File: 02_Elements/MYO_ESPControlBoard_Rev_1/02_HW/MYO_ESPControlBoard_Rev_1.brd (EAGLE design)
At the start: 408 x 156 mm, 55 parts, among them X1 USB-MICROB

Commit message: MYO_ESPControlBoard_Rev_1 Draft Update on HW (SCH, BRD and 3D)
Primary Draft of the PCB Schematic and Layout of MYO_ESPControlBoard_Rev_1, for evaluation:

- Complete Schematic
- Draft Layout without Drills or Silk
- Primary 3D Model
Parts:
- removed C_BUZZ: 30nF, adafruit:C0805K
- removed C_UR0: 10uF, adafruit:C0805K
- removed C_UR1: 100nF, adafruit:C0805K
- removed D1: MBRA140, SparkFun-DiscreteSemi:SMA-DIODE
- removed LED_PW1: (no value), adafruit:1206
- removed L_RGB_1: (no value), SparkFun-LED:WS2812B
- removed MOTPOT_2: POLOLU_MOT_POT, PololuMotors:POLOLU_MOT_POT
- removed R_BUZZ, R_PW1: 330Ohm, adafruit:M0805
- removed R_UR0, R_UR1: 470Ohm, adafruit:M0805
- removed R_UR2, R_UR3: 12KOhm, adafruit:M0805
- removed SW_KF, SW_KU: (no value), switch-omron:B3F-31XX
- removed T_UR0, T_UR1: S8050, semicon-smd-ipc:SOT23
- removed U_BUZZ: BUZZERSMD3, SparkFun:BUZZER-CMT1102
- removed U_UR0: CH340G, ch340g:SOIC16
- removed X_UR0: 12MHz, adafruit:CTS406
- added C_AS_0, C_AS_1: 22nF, adafruit:C0805K
- added R_AS_0, R_AS_1: 4k7Ohm, adafruit:M0805
- added R_SHUNT_0, R_SHUNT_1: 0.039Ohm, adafruit:M0805
- added R_SW_3: 10kOhm, adafruit:M0805
- added SW_00, SW_EN, SW_IO0: (no value), switch-omron:B3F-10XX
- added U_AS_0, U_AS_1: ZXCT1022E5TA, ZXCT1022E5TA:SOT95P270X145-5N(SOT23-5)
- U_DR_0, U_DR_1: value L293DD -> VNH7100ASTR; device st-microelectronics:SO20 -> VNH7100ASTR:SOIC127P600X175-16N
- X1: value USB-MICROB -> 332-04; device SparkFun:USB-MICROB -> con-garry:332-04
- moved R_AXL_0 479.0 mm to (48.0, 46.0)
- moved R_AXL_SCL 474.1 mm to (48.0, 43.0)
- moved R_AXL_SDA 469.4 mm to (48.0, 40.0)
- moved U_AXL 464.1 mm to (43.0, 45.0), turned to 270 degrees
- moved SW_PW 448.6 mm to (3.00, 23.0), flipped to the bottom, turned to 90 degrees
- moved J_PW 448.5 mm to (12.0, 19.0), flipped to the bottom, turned to 180 degrees
- moved C_ESP_1 443.9 mm to (11.0, 32.0), turned to 180 degrees
- moved R_SW_1 443.7 mm to (60.0, 10.0), turned to 180 degrees
- moved R_SW_0 431.2 mm to (49.0, 10.0), turned to 180 degrees
- moved L_RGB_0 419.6 mm to (5.00, 32.0), flipped to the bottom
- moved R_ESP2 301.4 mm to (43.0, 40.0)
- moved C_ESP_2 285.3 mm to (16.0, 29.0)
- moved C_ESP_3 285.0 mm to (11.0, 29.0), turned to 180 degrees
- moved R_ESP4 279.3 mm to (16.0, 26.0), turned to 180 degrees
- moved C_VR_2 271.8 mm to (36.0, 25.0), flipped to the bottom
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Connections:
- net GPIO15 renamed GPIO15(R)
- net GPIO2 renamed SWTAC_0
- net PMOT_A_3 renamed N$6
- removed net DTR: R_UR2.1, T_UR1.2, U_UR0.13
- removed net GPIO0: R_ESP0.1, R_SW_0.2, T_UR1.3, U_ESP.25
- removed net GPIO16: U_ESP.27
- removed net MOT_A_2: MOTPOT_2.MOT_A, U_DR_1.2, U_ESP.37
- removed net MOT_A_3: U_DR_1.12
- removed net MOT_B_2: MOTPOT_2.MOT_B, U_DR_1.9, U_ESP.10
- removed net MOT_B_3: U_DR_1.19
- removed net MOT_EN_2: U_DR_1.1, U_ESP.14
- removed net MOT_EN_3: U_DR_1.11
- removed net MPOT_2: MOTPOT_2.MPOT, U_ESP.9
- removed net N$10: L_RGB_0.2, L_RGB_1.4
- removed net N$12: R_UR0.1, U_UR0.2
- removed net N$13: R_UR1.1, U_UR0.3
- removed net N$14: U_UR0.8, X_UR0.3
- removed net N$15: D1.A, X1.VBUS
- removed net N$2: U_UR0.15
- removed net N$3: R_UR3.2, T_UR1.1
- removed net N$37: U_UR0.9
- removed net N$38: U_UR0.11
- removed net N$39: U_UR0.10
- removed net N$4: R_UR2.2, T_UR0.1
- removed net N$40: U_UR0.12
- removed net N$7: U_UR0.7, X_UR0.1
- removed net N$8: LED_PW1.A, R_PW1.1
- removed net N$9: L_RGB_1.2
- removed net PMOT_A_2: U_DR_1.3
- removed net PMOT_B_2: U_DR_1.8
- removed net PMOT_B_3: U_DR_1.18
- removed net RTS: R_UR3.1, T_UR0.2, U_UR0.14
- removed net USB_D+: U_UR0.5, X1.D+
- removed net USB_D-: U_UR0.6, X1.D-
- removed net _RST: T_UR0.3
- new net GPIO0(R): R_ESP0.1, R_SW_0.2, U_ESP.25
- new net GPIO23: U_ESP.37
- new net MOT_SEN_1: U_ESP.14
- new net MSEN_0: R_AS_0.1, U_ESP.9
- new net MSEN_1: R_AS_1.1
- new net N$11: C_AS_0.1, R_AS_0.2, U_AS_0.3
- new net N$42: C_AS_1.1, R_AS_1.2, U_AS_1.3
- new net RX: X1.3
- new net SW_0: R_SW_3.2, SW_00.3, U_ESP.27
- new net SW_1: MOTPOT_1.MOT_A, U_DR_1.3, U_ESP.16
- new net TX: X1.1
- new net VCC_VR_0: C_DR_0.1, R_SHUNT_0.2, R_SHUNT_1.2, U_AS_0.5, U_DR_0.12, U_DR_0.4, U_DR_0.5
- new net VCC_VR_1: C_DR_1.1, U_AS_1.5, U_DR_1.12, U_DR_1.4, U_DR_1.5
- net 3V3: now also R_SW_3.1, X1.2; no longer MOTPOT_2.3V3, R_PW1.2
- net 5V: now also R_SHUNT_0.1, R_SHUNT_1.1, U_AS_0.4, U_AS_1.4; no longer C_DR_0.1, C_DR_1.1, L_RGB_1.1, U_DR_0.10, U_DR_0.20, U_DR_1.10, U_DR_1.20
- net BUZZER: no longer R_BUZZ.2
- net GND: now also C_AS_0.2, C_AS_1.2, SW_00.1, SW_EN.1, SW_IO0.1, U_AS_0.2, U_AS_1.2, U_DR_0.1, U_DR_0.8, U_DR_0.9, U_DR_1.1, U_DR_1.8, U_DR_1.9, X1.4; no longer C_BUZZ.2, C_UR0.2, C_UR1.2, LED_PW1.C, L_RGB_1.3, MOTPOT_2.GND, SW_KF.2, SW_KU.2, U_BUZZ.2, U_DR_0.15, U_DR_0.17, U_DR_0.4, U_DR_0.5, U_DR_0.6, U_DR_0.7, U_DR_1.15, U_DR_1.17, U_DR_1.4, U_DR_1.5, U_DR_1.6, U_DR_1.7, U_UR0.1, X1.GND
- net MOT_A_0: now also U_DR_0.3; no longer U_DR_0.2
- net MOT_A_1: now also U_ESP.10; no longer MOTPOT_1.MOT_A, U_DR_0.12, U_ESP.16
- net MOT_B_0: now also U_DR_0.6; no longer U_DR_0.9
- net MOT_B_1: now also U_DR_1.6; no longer U_DR_0.19
- net MOT_EN_0: now also U_DR_0.11; no longer U_DR_0.1
- net MOT_EN_1: now also U_DR_1.11; no longer U_DR_0.11
- net N$1: now also U_DR_0.13; no longer C_BUZZ.1, R_BUZZ.1, U_BUZZ.1
- net N$18: now also SW_EN.3; no longer SW_KU.1
- net N$19: now also SW_IO0.3; no longer SW_KF.1
- net PMOT_A_0: now also U_DR_0.15, U_DR_0.2; no longer U_DR_0.3
- net PMOT_A_1: now also U_DR_1.15, U_DR_1.2; no longer U_DR_0.13
- net PMOT_B_0: now also U_DR_0.10, U_DR_0.7; no longer U_DR_0.8
- net PMOT_B_1: now also U_DR_1.10, U_DR_1.7; no longer U_DR_0.18
- net RXD: no longer R_UR1.2
- net TXD: no longer R_UR0.2
- net VIN: no longer C_UR0.1, C_UR1.1, D1.C, U_UR0.16
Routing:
- net GND: track 0.00 -> 330.0 mm, vias 0 -> 11
- net 3V3: track 0.00 -> 162.3 mm, vias 0 -> 6
- net 5V: track 0.00 -> 124.7 mm, vias 0 -> 3
- net VCC_VR_0: track 0.00 -> 117.4 mm, vias 0 -> 2
- net MOT_EN_0: track 0.00 -> 83.0 mm, vias 0 -> 2
- net MSEN_0: track 0.00 -> 74.8 mm, vias 0 -> 2
- net VIN: track 0.00 -> 73.3 mm, vias 0 -> 3
- net MPOT_0: track 0.00 -> 73.0 mm
- net MOT_A_0: track 0.00 -> 72.0 mm, vias 0 -> 6
- net MOT_EN_1: track 0.00 -> 70.2 mm
- net EN: track 0.00 -> 69.7 mm
- net MOT_B_0: track 0.00 -> 63.8 mm, vias 0 -> 5
- net SCL: track 0.00 -> 53.3 mm, vias 0 -> 3
- net GPIO0(R): track 0.00 -> 44.0 mm, vias 0 -> 3
- net SDA: track 0.00 -> 41.7 mm, vias 0 -> 4
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- removed copper zone on layer 1, net GND
- removed copper zone on layer 16, net GND
- removed copper zone on layer 16, net N$11
- removed copper zone on layer 1, net N$6 (its old number)
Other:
- board size 408 x 156 mm -> 72 x 57 mm
- board text removed: "Add a dissipator to avoid overheating"
- board text removed: "BOT:"
- board text removed: "C:/Users/PablodMM/Google Drive/Henar #3/03_Recursos/License_3_0_Logo.bmp"
- board text removed: "C_MUX_0"
- board text removed: "C_MUX_1"
- board text removed: "C_VR_1"
- board text removed: "Check the Fuse in case the board is not powered"
- board text removed: "F_PW"
- board text removed: "GND 5V RX TX"
- board text removed: "GND 5V_ARD MUX_D MUX_C MUX_B MUX_A MUX_2"
- board text removed: "H3_MIDIController_Rev_3_MainBoard"
- board text removed: "J_MIDI"
- board text removed: "J_SW_00"
- board text removed: "J_SW_01"
- board text removed: "J_SW_02"
- board text removed: "J_SW_03"
- board text removed: "J_SW_04"
- board text removed: "J_SW_05"
- board text removed: "J_SW_06"
- board text removed: "J_SW_07"
- board text removed: "J_SW_08"
- board text removed: "J_SW_09"
- board text removed: "J_SW_10"
- board text removed: "J_SW_11"
- board text removed: "J_SW_12"
- board text removed: "J_SW_13"
- board text removed: "J_SW_14"
- board text removed: "J_SW_15"
- board text removed: "J_SW_16"
- board text removed: "J_SW_17"
- board text removed: "J_SW_18"
- board text removed: "J_SW_19"
- board text removed: "J_SW_20"
- board text removed: "J_SW_21"
- board text removed: "J_SW_22"
- board text removed: "J_SW_23"
- board text removed: "J_SW_24"
- board text removed: "J_SW_25"
- board text removed: "J_SW_26"
- board text removed: "J_SW_27"
- board text removed: "J_SW_28"
- board text removed: "J_SW_29"
- board text removed: "J_SW_30"
- board text removed: "J_SW_31"
- board text removed: "LED_IN LED_OUT 5V GND SW_00"
- board text removed: "LED_IN LED_OUT 5V GND SW_01"
- board text removed: "LED_IN LED_OUT 5V GND SW_02"
- board text removed: "LED_IN LED_OUT 5V GND SW_03"
- board text removed: "LED_IN LED_OUT 5V GND SW_04"
- board text removed: "LED_IN LED_OUT 5V GND SW_05"
- board text removed: "LED_IN LED_OUT 5V GND SW_06"
- board text removed: "LED_IN LED_OUT 5V GND SW_07"
- board text removed: "LED_IN LED_OUT 5V GND SW_08"
- board text removed: "LED_IN LED_OUT 5V GND SW_09"
- board text removed: "LED_IN LED_OUT 5V GND SW_10"
- board text removed: "LED_IN LED_OUT 5V GND SW_13"
- board text removed: "LED_IN LED_OUT 5V GND SW_14"
- board text removed: "LED_IN LED_OUT 5V GND SW_15"
- board text removed: "LED_IN LED_OUT 5V GND SW_16"
- board text removed: "LED_IN LED_OUT 5V GND SW_17"
- board text removed: "LED_IN LED_OUT 5V GND SW_18"
- board text removed: "LED_IN LED_OUT 5V GND SW_19"
- board text removed: "LED_IN LED_OUT 5V GND SW_20"
- board text removed: "LED_IN LED_OUT 5V GND SW_21"
- board text removed: "LED_IN LED_OUT 5V GND SW_22"
- board text removed: "LED_IN LED_OUT 5V GND SW_23"
- board text removed: "LED_IN LED_OUT 5V GND SW_24"
- board text removed: "LED_IN LED_OUT 5V GND SW_25"
- board text removed: "LED_IN LED_OUT 5V GND SW_26"
- board text removed: "LED_IN LED_OUT 5V GND SW_29"
- board text removed: "LED_IN LED_OUT 5V GND SW_30"
- board text removed: "LED_IN LED_OUT 5V GND SW_31"
- board text removed: "LED_PW"
- board text removed: "LED_RGB"
- board text removed: "Licensed CC BY-SA 3.0"
- board text removed: "Multiplexer 16to1 MUX_0"
- board text removed: "Multiplexer 16to1 MUX_1"
- board text removed: "RAW(NC) GND RST(NC) 5V_ARD A3(NC) MUX_2 MUX_1 MUX_0 D13(NC) D12(NC) D11(NC) D10(NC)"
- board text removed: "R_LED_B"
- board text removed: "R_LED_G"
- board text removed: "R_LED_R"
- board text removed: "R_MIDI_0"
- board text removed: "R_MIDI_1"
- board text removed: "R_MIDI_2"
- board text removed: "R_PW"
- board text removed: "SWPad 00"
- board text removed: "SWPad 01"
- board text removed: "SWPad 02"
- board text removed: "SWPad 03"
- board text removed: "SWPad 04"
- board text removed: "SWPad 05"
- board text removed: "SWPad 06"
- board text removed: "SWPad 07"
- board text removed: "SWPad 08"
- board text removed: "SWPad 09"
- board text removed: "SWPad 10"
- board text removed: "SWPad 11"
- board text removed: "SWPad 12"
- board text removed: "SWPad 13"
- board text removed: "SWPad 14"
- board text removed: "SWPad 15"
- board text removed: "SWPad 16"
- board text removed: "SWPad 17"
- board text removed: "SWPad 18"
- board text removed: "SWPad 19"
- board text removed: "SWPad 20"
- board text removed: "SWPad 21"
- board text removed: "SWPad 22"
- board text removed: "SWPad 23"
- board text removed: "SWPad 24"
- board text removed: "SWPad 25"
- board text removed: "SWPad 26"
- board text removed: "SWPad 27"
- board text removed: "SWPad 28"
- board text removed: "SWPad 29"
- board text removed: "SWPad 30"
- board text removed: "SWPad 31"
- board text removed: "Spain, 2017"
- board text removed: "TX RX 5V GND"
- board text removed: "U_MUX_0"
- board text removed: "U_MUX_1"
- board text removed: "U_VR_5V"
- board text removed: "VIN GND VOUT"

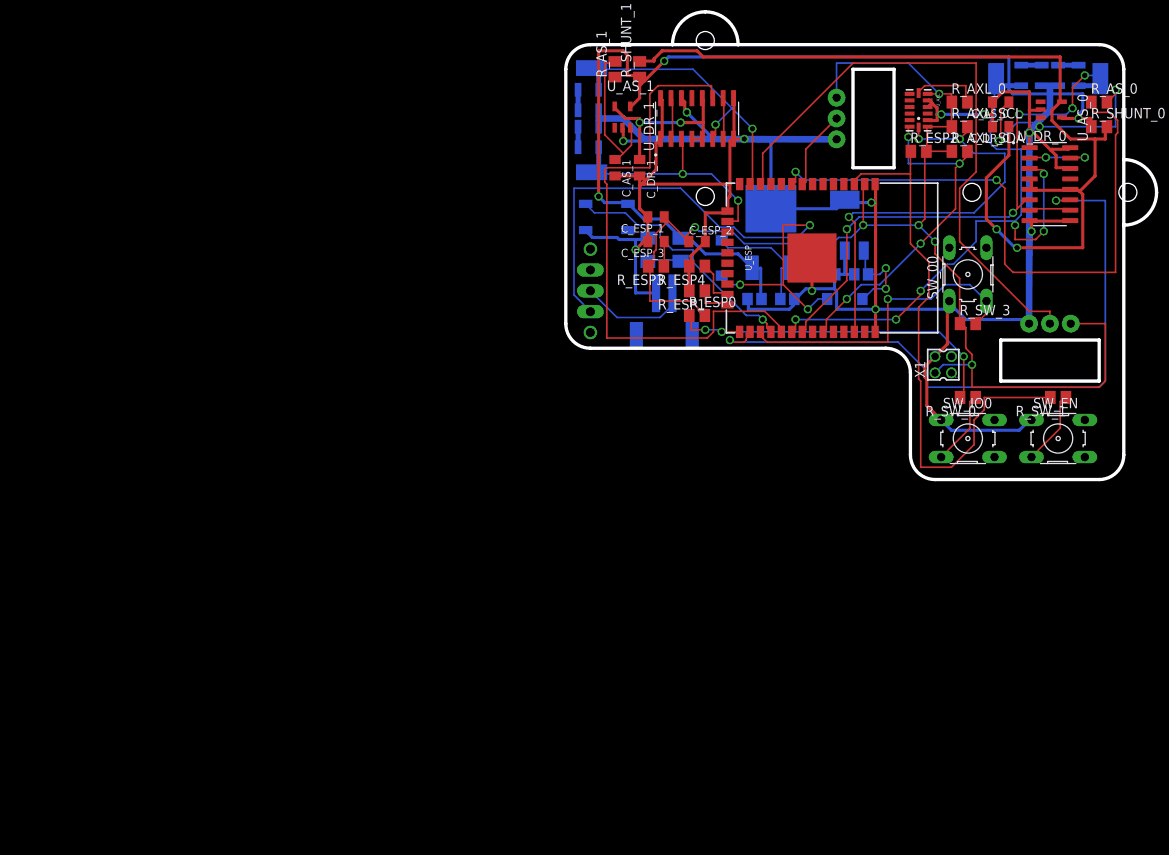
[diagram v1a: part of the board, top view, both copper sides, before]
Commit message: Updated Design with NPN JTAG Programming Interface
Changed Schematic:

- Added NPN JTAG Controller (as for https://dl.espressif.com/dl/schematics/ESP32-Core-Board-V2_sch.pdf ). Suppresed 2 Tactile Switches for Programming Interface
- Added 1 Tactile Switch for User Interface
- Added Expressiv Documentation
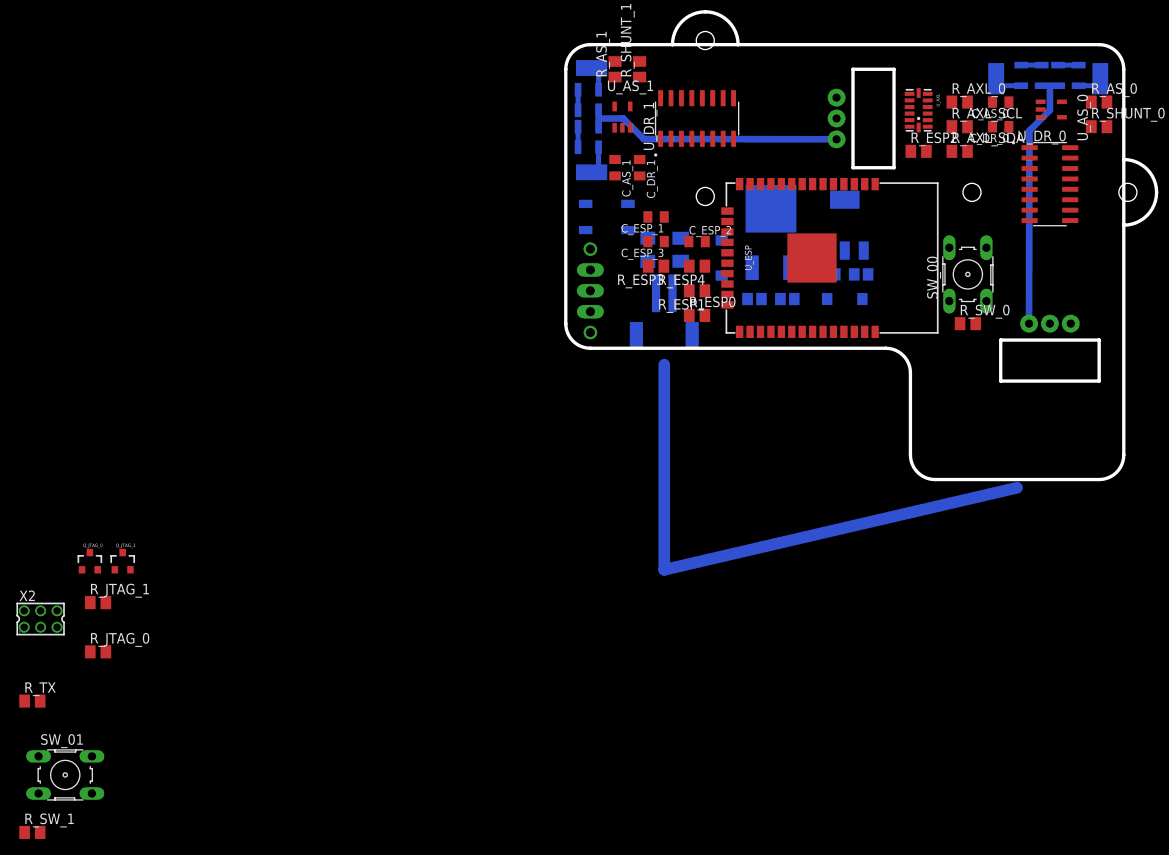
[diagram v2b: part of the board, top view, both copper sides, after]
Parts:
- removed R_SW_3: 10kOhm, adafruit:M0805
- removed SW_EN, SW_IO0: (no value), switch-omron:B3F-10XX
- removed X1: 332-04, con-garry:332-04
- added Q_JTAG_0, Q_JTAG_1: (no value), SparkFun:SOT23-3
- added R_JTAG_0, R_JTAG_1: 12KOhm, adafruit:M0805
- added R_TX: 470Ohm, adafruit:M0805
- added SW_01: (no value), switch-omron:B3F-10XX
- added X2: 332-06, con-garry:332-06
- R_SW_0, R_SW_1: value 470Ohm -> 10kOhm
- moved R_SW_1 135.8 mm to (-65.0, -43.0), turned to 0 degrees
- moved R_SW_0 9.00 mm to (49.0, 19.0), turned to 0 degrees
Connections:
- removed net GPIO23: U_ESP.37
- removed net N$18: R_SW_1.1, SW_EN.3
- removed net N$19: R_SW_0.1, SW_IO0.3
- new net DTR: Q_JTAG_1.2, R_JTAG_0.1, X2.6
- new net N$4: Q_JTAG_0.1, R_JTAG_0.2
- new net N$7: Q_JTAG_1.1, R_JTAG_1.2
- new net N$9: R_TX.1, X2.4
- new net RTS: Q_JTAG_0.2, R_JTAG_1.1, X2.5
- net 3V3: now also R_SW_0.1, R_SW_1.1, X2.2; no longer R_SW_3.1, X1.2
- net EN: now also Q_JTAG_0.3; no longer R_SW_1.2
- net GND: now also SW_01.1, X2.1; no longer SW_EN.1, SW_IO0.1, X1.4
- net GPIO0(R): now also Q_JTAG_1.3; no longer R_SW_0.2
- net RX: now also X2.3; no longer X1.3
- net SW_0: now also R_SW_0.2; no longer R_SW_3.2
- net SW_1: now also R_SW_1.2, SW_01.3, U_ESP.37
- net TX: now also R_TX.2; no longer X1.1
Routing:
- net GND: track 330.0 -> 0.00 mm, vias 11 -> 0
- net 3V3: track 162.3 -> 0.00 mm, vias 6 -> 0
- net 5V: track 124.7 -> 0.00 mm, vias 3 -> 0
- net VCC_VR_0: track 117.4 -> 0.00 mm, vias 2 -> 0
- net MOT_EN_0: track 83.0 -> 0.00 mm, vias 2 -> 0
- net MSEN_0: track 74.8 -> 0.00 mm, vias 2 -> 0
- net VIN: track 73.3 -> 0.00 mm, vias 3 -> 0
- net MPOT_0: track 73.0 -> 0.00 mm
- net MOT_A_0: track 72.0 -> 0.00 mm, vias 6 -> 0
- net MOT_EN_1: track 70.2 -> 0.00 mm
- net EN: track 69.7 -> 0.00 mm
- net MOT_B_0: track 63.8 -> 0.00 mm, vias 5 -> 0
- net SCL: track 53.3 -> 0.00 mm, vias 3 -> 0
- net N$3: track 0.00 -> 44.1 mm
- net GPIO0(R): track 44.0 -> 0.00 mm, vias 3 -> 0
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
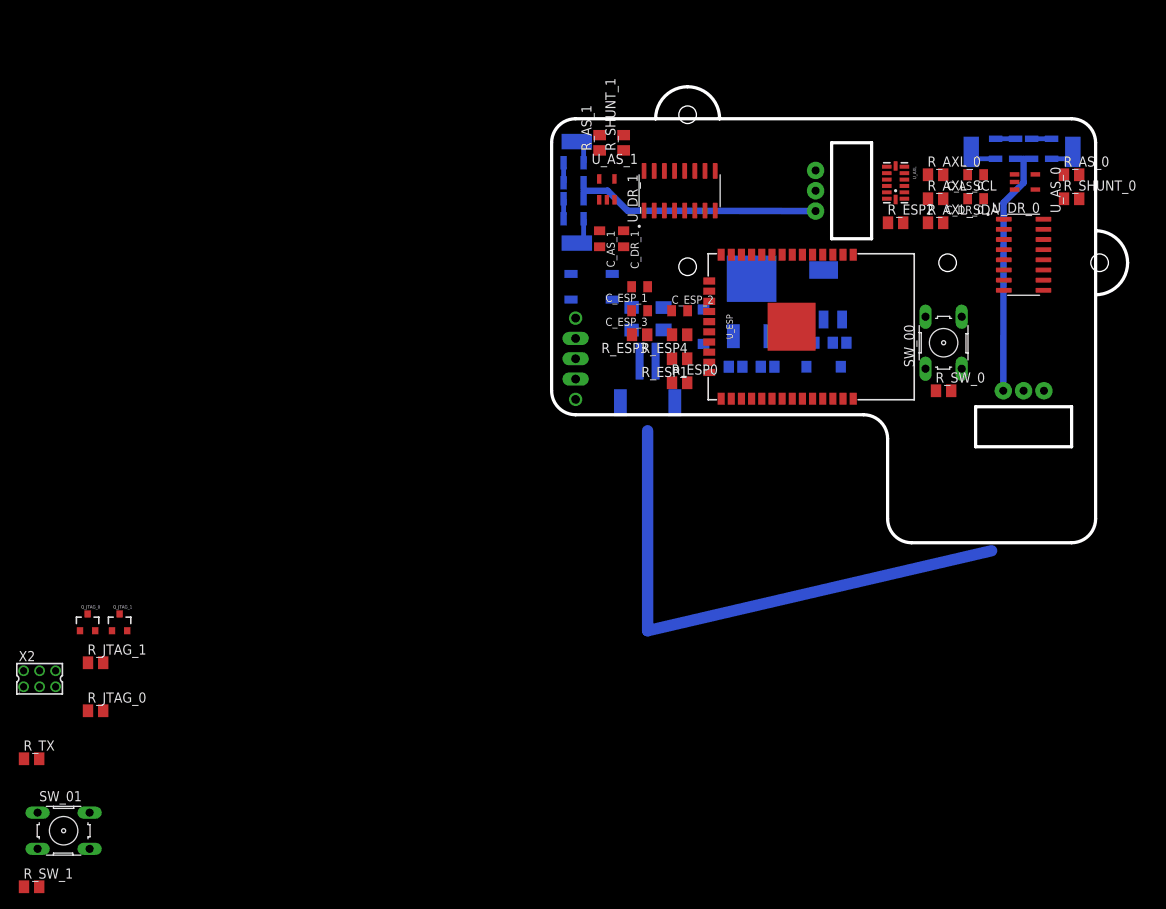
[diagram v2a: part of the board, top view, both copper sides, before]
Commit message: MYO_ESPControlBoard_Rev_1 Schematic Fixed. New Dimensions for Board
MYO_ESPControlBoard_Rev_1:

- Schematic Fixed
- Tactile Switch SW_1 Removed
- New Dimensions and Board Layout

Transition Commit, soon to be finished :-)
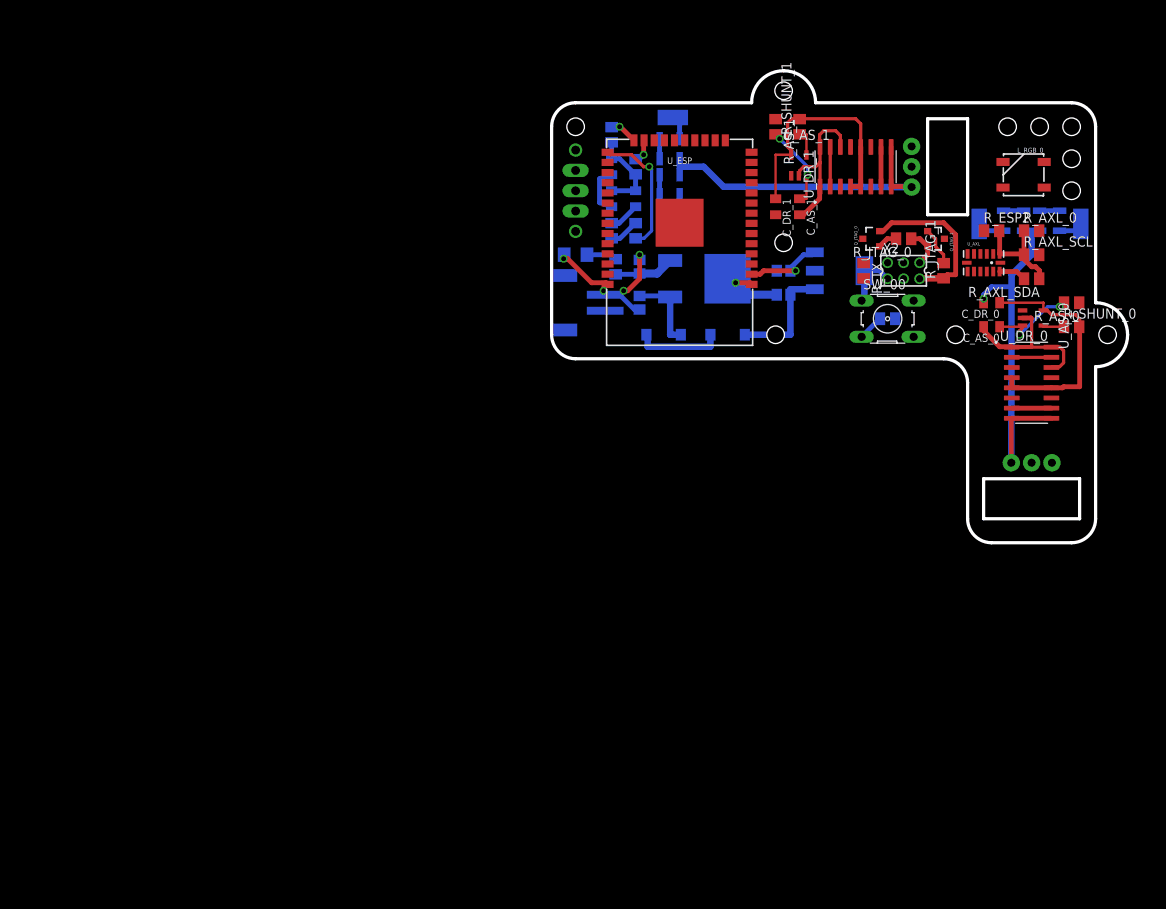
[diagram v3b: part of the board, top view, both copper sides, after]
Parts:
- removed R_SW_1: 10kOhm, adafruit:M0805
- removed SW_01: (no value), switch-omron:B3F-10XX
- R_PW: device adafruit:M1206 -> adafruit:M0805
- moved R_TX 120.6 mm to (39.0, 34.0), turned to 270 degrees
- moved X2 119.4 mm to (44.0, 34.0)
- moved R_JTAG_0 117.0 mm to (44.0, 38.0), turned to 180 degrees
- moved R_JTAG_1 116.8 mm to (49.0, 34.0), turned to 90 degrees
- moved Q_JTAG_1 112.7 mm to (48.0, 38.0), turned to 270 degrees
- moved Q_JTAG_0 109.1 mm to (40.0, 38.0), turned to 90 degrees
- moved L_RGB_0 55.8 mm to (59.0, 46.0), flipped to the top, turned to 180 degrees
- moved R_ESP1 29.3 mm to (7.50, 51.0), flipped to the bottom, turned to 270 degrees
- moved C_AS_1 25.3 mm to (31.0, 42.0)
- moved U_AS_1 24.2 mm to (31.0, 47.0)
- moved U_DR_1 22.2 mm to (38.0, 47.0)
- moved R_AS_1 22.1 mm to (28.0, 52.0), turned to 270 degrees
- moved R_SHUNT_1 22.1 mm to (31.0, 52.0)
- moved R_ESP4 21.7 mm to (10.5, 47.0), flipped to the bottom, turned to 270 degrees
- moved SW_PW 21.0 mm to (3.00, 44.0)
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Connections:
- removed net N$32: U_ESP.6
- removed net RX: X2.3
- removed net SW_1: MOTPOT_1.MOT_A, R_SW_1.2, SW_01.3, U_DR_1.3, U_ESP.16, U_ESP.37
- removed net TX: R_TX.2
- new net GPIO13: U_ESP.16
- new net GPIO23: U_ESP.37
- net 3V3: no longer R_SW_1.1
- net GND: no longer SW_01.1
- net MOT_A_0: no longer MOTPOT_0.MOT_A
- net MOT_A_1: now also U_DR_1.3
- net MOT_B_0: no longer MOTPOT_0.MOT_B
- net MOT_B_1: no longer MOTPOT_1.MOT_B
- net MSEN_1: now also U_ESP.6
- net PMOT_A_0: now also MOTPOT_0.MOT_A
- net PMOT_A_1: now also MOTPOT_1.MOT_A
- net PMOT_B_0: now also MOTPOT_0.MOT_B
- net PMOT_B_1: now also MOTPOT_1.MOT_B
- net RXD: now also X2.3
- net TXD: now also R_TX.2
- net VCC_VR_0: no longer R_SHUNT_1.2
- net VCC_VR_1: now also R_SHUNT_1.2
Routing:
- net GND: track 0.00 -> 116.1 mm, vias 0 -> 6
- net N$3: track 44.1 -> 0.00 mm
- net 3V3: track 0.00 -> 34.5 mm, vias 0 -> 1
- net VCC_VR_1: track 0.00 -> 30.4 mm
- net VCC_VR_0: track 0.00 -> 29.8 mm
- net N$2: track 25.0 -> 1.00 mm
- net RTS: track 0.00 -> 20.3 mm
- net GPIO0(R): track 0.00 -> 16.5 mm, vias 0 -> 1
- net V33: track 0.00 -> 14.4 mm
- net 5V: track 0.00 -> 13.7 mm
- net N$11: track 0.00 -> 11.5 mm, vias 0 -> 2
- net VIN: track 0.00 -> 11.0 mm
- net N$42: track 0.00 -> 10.6 mm, vias 0 -> 2
- net V5: track 0.00 -> 9.92 mm
- net PMOT_B_1: track 0.00 -> 4.95 mm
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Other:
- board size 72 x 57 mm -> 72 x 59 mm

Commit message: Updated Schematic and Board
Safe Bakcup
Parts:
- removed R_ESP3: 12KOhm, adafruit:M0805
- R_ESP0, R_ESP1: value 12KOhm -> 5KOhm
- moved U_DR_1 83.2 mm to (-45.0, 52.0), turned to 270 degrees
- moved L_RGB_0 74.6 mm to (-2.00, 3.00)
- moved U_DR_0 73.6 mm to (-13.0, 11.0)
- moved C_AS_0 73.2 mm to (-18.0, 21.0)
- moved C_DR_0 73.2 mm to (-18.0, 24.0)
- moved R_AS_0 73.2 mm to (-8.00, 24.0)
- moved R_AXL_0 73.2 mm to (-13.0, 33.0)
- moved R_AXL_SCL 73.2 mm to (-13.0, 30.0)
- moved R_AXL_SDA 73.2 mm to (-13.0, 27.0)
- moved R_ESP2 73.2 mm to (-18.0, 33.0)
- moved R_SHUNT_0 73.2 mm to (-8.00, 21.0)
- moved U_AS_0 73.2 mm to (-13.0, 22.0)
- moved U_AXL 73.2 mm to (-19.0, 29.0)
- moved SW_00 73.0 mm to (-25.0, -1.00), turned to 90 degrees
- moved C_AS_1 69.6 mm to (-37.0, 57.0), turned to 90 degrees
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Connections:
- net BUZZER renamed GPIO26
- net MOT_SEN_1 renamed GPIO12
- removed net NRST: C_ESP_3.1, R_ESP3.1
- new net GPIO2: U_ESP.24
- net 3V3: no longer R_ESP3.2
- net EN: now also C_ESP_3.1
- net SWTAC_0: no longer U_ESP.24
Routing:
- net GND: track 116.1 -> 0.00 mm, vias 6 -> 0
- net 3V3: track 34.5 -> 0.00 mm, vias 1 -> 0
- net VCC_VR_1: track 30.4 -> 0.00 mm
- net VCC_VR_0: track 29.8 -> 0.00 mm
- net RTS: track 20.3 -> 0.00 mm
- net GPIO0(R): track 16.5 -> 0.00 mm, vias 1 -> 0
- net V33: track 14.4 -> 0.00 mm
- net 5V: track 13.7 -> 0.00 mm
- net N$11: track 11.5 -> 0.00 mm, vias 2 -> 0
- net VIN: track 11.0 -> 0.00 mm
- net N$42: track 10.6 -> 0.00 mm, vias 2 -> 0
- net V5: track 9.92 -> 0.00 mm
- net PMOT_B_1: track 4.95 -> 0.00 mm
- net PMOT_B_0: track 4.95 -> 0.00 mm
- net PMOT_A_1: track 4.95 -> 0.00 mm
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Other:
- board size 72 x 59 mm -> 72 x 49 mm
